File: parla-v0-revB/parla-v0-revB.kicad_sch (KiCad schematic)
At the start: 16 parts, among them J1 AudioJack2_SwitchT, J2 AudioJack2_SwitchT, J3 AudioJack2_SwitchT, J4 AudioJack2_SwitchT, U1 PAM8403D

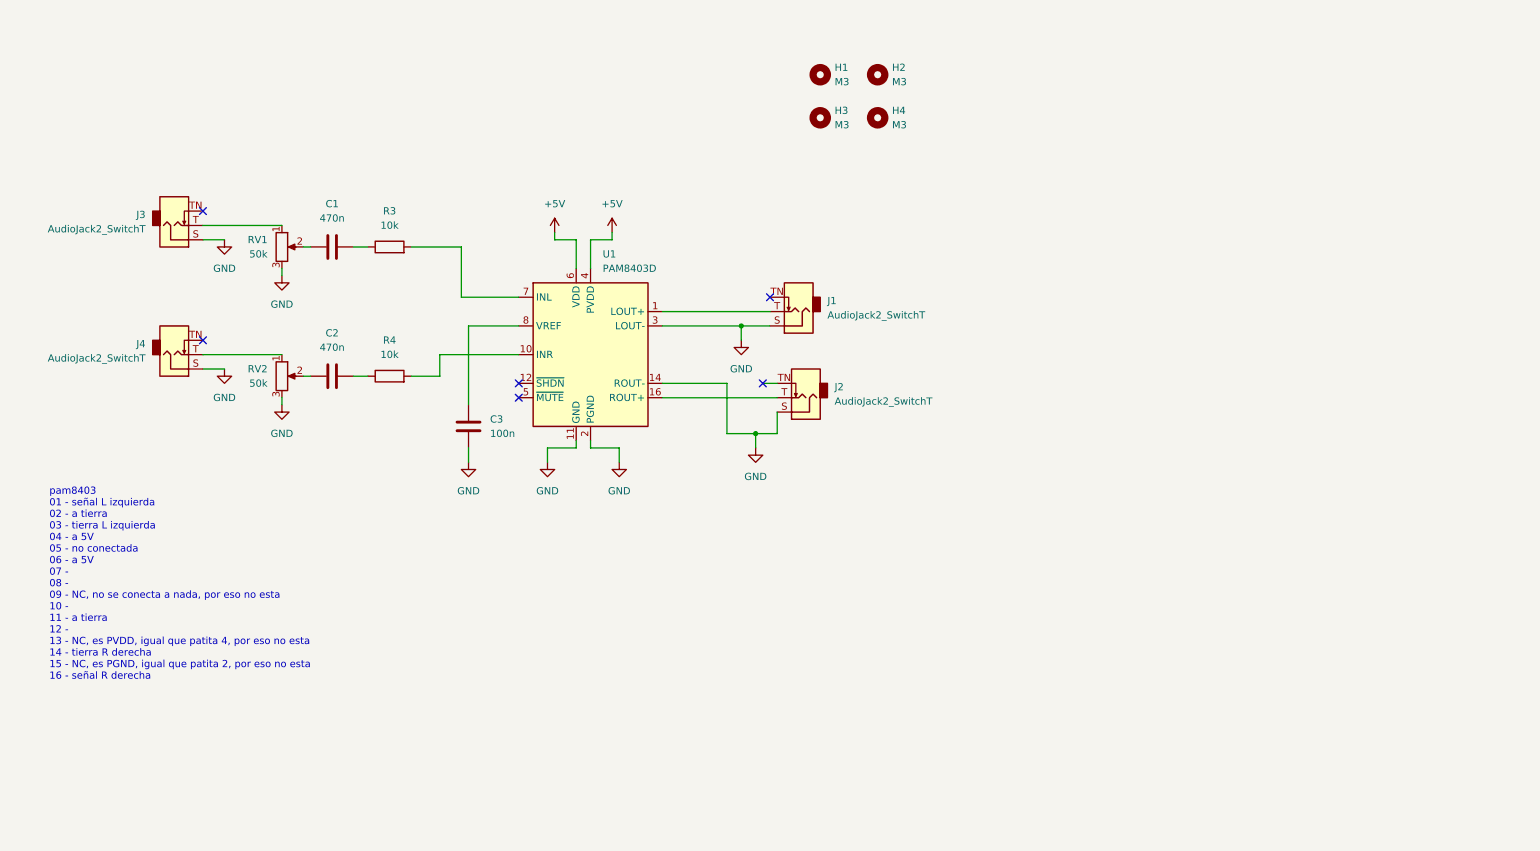
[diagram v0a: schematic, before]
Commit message: agregar vias
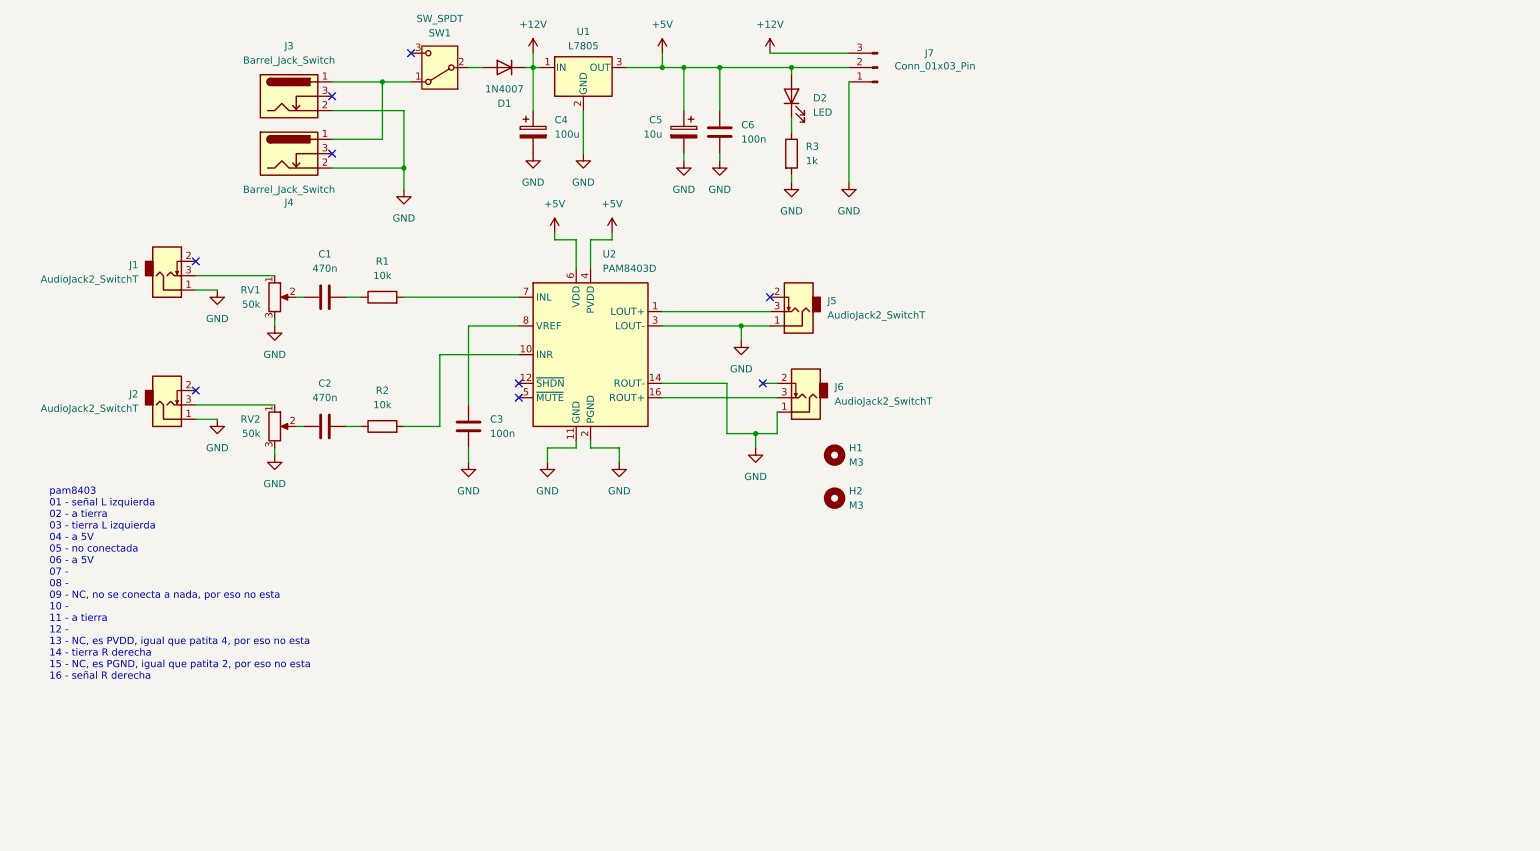
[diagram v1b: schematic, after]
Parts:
- removed H2, H4: M3, MountingHole:MountingHole_3.2mm_M3, symbol Mechanical:MountingHole
- added C4: 100u, Capacitor_THT:CP_Radial_D8.0mm_P3.80mm, symbol Device:C_Polarized
- added C5: 10u, Capacitor_THT:CP_Radial_D4.0mm_P2.00mm, symbol Device:C_Polarized
- added C6: 100n, Capacitor_THT:C_Disc_D5.0mm_W2.5mm_P2.50mm, symbol Device:C
- added D1: 1N4007, Diode_THT:D_DO-41_SOD81_P10.16mm_Horizontal, symbol Diode:1N4007
- added D2: LED, LED_THT:LED_D5.0mm, symbol Device:LED
- added J3, J4: Barrel_Jack_Switch, Connector_BarrelJack:BarrelJack_Horizontal, symbol Connector:Barrel_Jack_Switch
- added J7: Conn_01x03_Pin, Connector_PinSocket_2.54mm:PinSocket_1x03_P2.54mm_Vertical, symbol Connector:Conn_01x03_Pin
- added R3: 1k, Resistor_THT:R_Axial_DIN0207_L6.3mm_D2.5mm_P10.16mm_Horizontal, symbol Device:R
- added SW1: SW_SPDT, parla:spdt_ssd12d00g3, symbol Switch:SW_SPDT
- added U1: L7805, Package_TO_SOT_THT:TO-220-3_Horizontal_TabDown, symbol Regulator_Linear:L7805
- C1, C2, C3: footprint (none) -> Capacitor_THT:C_Disc_D5.0mm_W2.5mm_P2.50mm
- J1: renamed from J3; footprint (none) -> parla:PJ301M-12
- J2: renamed from J4; footprint (none) -> parla:PJ301M-12
- J5: renamed from J1; footprint (none) -> parla:PJ301M-12
- J6: renamed from J2; footprint (none) -> parla:PJ301M-12
- R1: renamed from R3; footprint (none) -> Resistor_THT:R_Axial_DIN0207_L6.3mm_D2.5mm_P10.16mm_Horizontal
- R2: renamed from R4; footprint (none) -> Resistor_THT:R_Axial_DIN0207_L6.3mm_D2.5mm_P10.16mm_Horizontal
- RV1, RV2: footprint (none) -> Potentiometer_THT:Potentiometer_Alps_RK163_Single_Horizontal
- renumbered H3 to H2, U1 to U2
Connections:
- net +5V: now also C5.1, C6.1, D2.2 (A), J7.2 (Pin_2), U1.3 (OUT)
- net GND: now also J1.1, J2.1, J5.1, J6.1, C4.2, C5.2, C6.2, J3.2, J4.2, J7.1 (Pin_1), R3.2, U1.2 (GND); no longer J1.S, J2.S, J5.S, J6.S
- net at U2.1 (LOUT+): now also J5.3; no longer J5.T
- net at U2.16 (ROUT+): now also J6.3; no longer J6.T
- net at RV1.1: now also J1.3; no longer J1.T
- net at RV2.1: now also J2.3; no longer J2.T
- new net: D2.1 (K), R3.1
- new net: J3.1, J4.1, SW1.1 (A)
- new net: D1.2 (A), SW1.2 (B)
- new net +12V: C4.1, D1.1 (K), J7.3 (Pin_3), U1.1 (IN)
- no-connect marks 6 -> 9
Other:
- title: parla-v0.1.0 -> parla
- moved on the sheet: C1, C2, H1, H2, J1, J2, R1, R2, RV1, RV2

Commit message: nueva version matias
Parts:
- removed C4: 100u, Capacitor_THT:CP_Radial_D8.0mm_P3.80mm, symbol Device:C_Polarized
- removed C5: 10u, Capacitor_THT:CP_Radial_D4.0mm_P2.00mm, symbol Device:C_Polarized
- removed D2: LED, LED_THT:LED_D5.0mm, symbol Device:LED
- removed J3, J4: Barrel_Jack_Switch, Connector_BarrelJack:BarrelJack_Horizontal, symbol Connector:Barrel_Jack_Switch
- removed J7: Conn_01x03_Pin, Connector_PinSocket_2.54mm:PinSocket_1x03_P2.54mm_Vertical, symbol Connector:Conn_01x03_Pin
- removed R3: 1k, Resistor_THT:R_Axial_DIN0207_L6.3mm_D2.5mm_P10.16mm_Horizontal, symbol Device:R
- removed SW1: SW_SPDT, parla:spdt_ssd12d00g3, symbol Switch:SW_SPDT
- removed U1: L7805, Package_TO_SOT_THT:TO-220-3_Horizontal_TabDown, symbol Regulator_Linear:L7805
- added C10: 100n, Capacitor_SMD:C_0805_2012Metric_Pad1.18x1.45mm_HandSolder, symbol Device:C
- added C4, C5: 1u, Capacitor_SMD:C_0805_2012Metric_Pad1.18x1.45mm_HandSolder, symbol Device:C
- added C7: 100u, Capacitor_SMD:CP_Elec_6.3x7.7, symbol Device:C_Polarized
- added C8: 220u, Capacitor_SMD:CP_Elec_6.3x5.4, symbol Device:C_Polarized
- added C9: 10u, Capacitor_SMD:CP_Elec_4x5.4, symbol Device:C_Polarized
- added D8: LED, LED_THT:LED_D5.0mm, symbol Device:LED
- added H2, H4: M3, MountingHole:MountingHole_3.2mm_M3, symbol Mechanical:MountingHole
- added J5: Barrel_Jack_Switch, Connector_BarrelJack:BarrelJack_Horizontal, symbol Connector:Barrel_Jack_Switch
- added R5: 1k, Resistor_SMD:R_0805_2012Metric_Pad1.20x1.40mm_HandSolder, symbol Device:R
- added SW3: SW_SPDT, dis8644:spdt_ssd12d00g3, symbol Switch:SW_SPDT
- added U2: L7805, Package_TO_SOT_SMD:TO-252-2, symbol Regulator_Linear:L7805
- C1, C2: footprint Capacitor_THT:C_Disc_D5.0mm_W2.5mm_P2.50mm -> Capacitor_SMD:C_Elec_4x5.4; LCSC (none) -> C2895732
- C3: footprint Capacitor_THT:C_Disc_D5.0mm_W2.5mm_P2.50mm -> Capacitor_SMD:C_0805_2012Metric_Pad1.18x1.45mm_HandSolder; LCSC (none) -> C49678
- C6: value 100n -> 1u; footprint Capacitor_THT:C_Disc_D5.0mm_W2.5mm_P2.50mm -> Capacitor_SMD:C_0805_2012Metric_Pad1.18x1.45mm_HandSolder; LCSC (none) -> C77083
- D1: footprint Diode_THT:D_DO-41_SOD81_P10.16mm_Horizontal -> Diode_SMD:D_SOD-323_HandSoldering; LCSC (none) -> C193404
- J1: renamed from J5; footprint parla:PJ301M-12 -> dis8644:PJ301M-12-T_TN_S
- J2: renamed from J6; footprint parla:PJ301M-12 -> dis8644:PJ301M-12-T_TN_S
- J3: renamed from J1; footprint parla:PJ301M-12 -> dis8644:PJ301M-12-T_TN_S
- J4: renamed from J2; footprint parla:PJ301M-12 -> dis8644:PJ301M-12-T_TN_S
- R3: renamed from R1; footprint Resistor_THT:R_Axial_DIN0207_L6.3mm_D2.5mm_P10.16mm_Horizontal -> Resistor_SMD:R_0805_2012Metric_Pad1.20x1.40mm_HandSolder; LCSC (none) -> C17414
- R4: renamed from R2; footprint Resistor_THT:R_Axial_DIN0207_L6.3mm_D2.5mm_P10.16mm_Horizontal -> Resistor_SMD:R_0805_2012Metric_Pad1.20x1.40mm_HandSolder; LCSC (none) -> C17414
- RV1, RV2: footprint Potentiometer_THT:Potentiometer_Alps_RK163_Single_Horizontal -> Potentiometer_THT:Potentiometer_Bourns_PTV09A-1_Single_Vertical
- U1: renamed from U2; LCSC (none) -> C5122557
- renumbered H2 to H3
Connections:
- net +12V: now also C7.1, U2.1 (IN)
- net +5V: now also C6.2, C10.1, C4.2, C5.2, C8.1, C9.1, D8.2 (A), U2.3 (OUT); no longer C6.1
- net GND: now also C6.1, J1.S, J2.S, J3.S, J4.S, C10.2, C4.1, C5.1, C7.2, C8.2, C9.2, J5.2, R5.1, U2.2 (GND); no longer C6.2, J1.1, J2.1, J3.1, J4.1
- net at U1.1 (LOUT+): now also J1.T; no longer J1.3
- net at U1.16 (ROUT+): now also J2.T; no longer J2.3
- net at RV1.1: now also J3.T; no longer J3.3
- net at D1.2 (A): now also SW3.2 (B)
- net at RV2.1: now also J4.T; no longer J4.3
- new net: D8.1 (K), R5.2
- new net: J5.1, SW3.1 (A)
- no-connect marks 9 -> 8
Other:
- note added: "ALIMENTACIÓN"
- note added: "FUENTES ENTRE 7 y 12V Centro positivo"
- note added: "PIN 3 = 12v PIN 2 = 5v PIN 1 = GND"
- note added: "TODOS LOS CHIPS DEBEN SER ALIMENTADOS CON 5V"
- title: parla -> parla-v0.1.0
- moved on the sheet: C1, H1, H3, J3, J4, R3, R4, RV1, RV2

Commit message: editadas huellas standard
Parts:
- C7: footprint Capacitor_SMD:CP_Elec_6.3x7.7 -> Capacitor_SMD:CP_Elec_5x5.4; LCSC C72478 -> C3347
- C8: footprint Capacitor_SMD:CP_Elec_6.3x5.4 -> Capacitor_SMD:CP_Elec_6.3x7.7; LCSC C72494 -> C3342
- C9: LCSC C72485 -> C3357
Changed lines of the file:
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@@
 			)
 		)
-		(property "Footprint" "Capacitor_SMD:CP_Elec_6.3x7.7"
+		(property "Footprint" "Capacitor_SMD:CP_Elec_5x5.4"
 			(at 154.6352 147.955 0)
 			(hide yes)
@@
 			)
 		)
-		(property "LCSC" "C72478"
+		(property "LCSC" "C3347"
 			(at 153.67 144.145 0)
 			(hide yes)
@@
 			)
 		)
-		(property "Footprint" "Capacitor_SMD:CP_Elec_6.3x5.4"
+		(property "Footprint" "Capacitor_SMD:CP_Elec_6.3x7.7"
 			(at 137.4902 31.115 0)
 			(hide yes)
@@
 			)
 		)
-		(property "LCSC" "C72494"
+		(property "LCSC" "C3342"
 			(at 136.525 27.305 0)
 			(hide yes)
@@
 			)
 		)
-		(property "LCSC" "C72485"
+		(property "LCSC" "C3357"
 			(at 179.07 144.145 0)
 			(hide yes)
